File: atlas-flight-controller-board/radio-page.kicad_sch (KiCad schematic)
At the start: 1 part

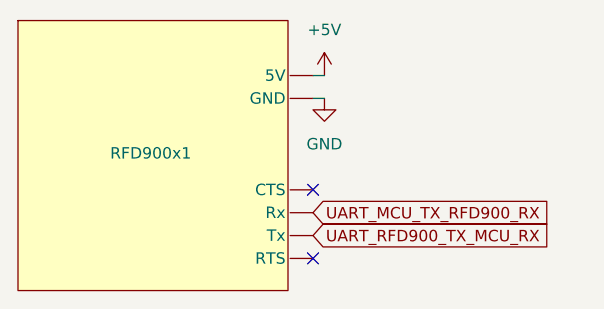
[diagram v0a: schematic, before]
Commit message: Added Regulator, Leaving disconnected, and off pcb for now as teensy board does this automatically. Leaving on for future revs without teensy board
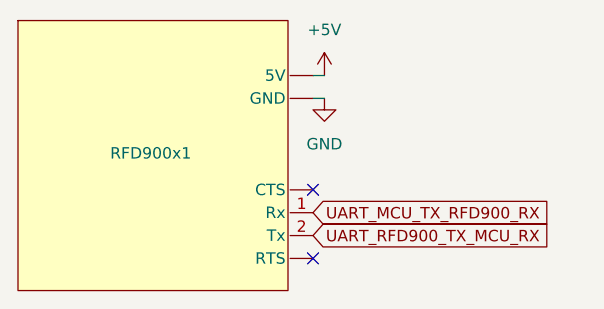
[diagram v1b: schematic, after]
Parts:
- RFD900x1: footprint (none) -> TerminalBlock:TerminalBlock_Xinya_XY308-2.54-2P_1x02_P2.54mm_Horizontal
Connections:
- net UART_MCU_TX_RFD900_RX: now also RFD900x1.1 (Rx); no longer RFD900x1. (RTS)
- net UART_RFD900_TX_MCU_RX: now also RFD900x1.2 (Tx); no longer RFD900x1. (RTS)
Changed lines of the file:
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@@
 			)
 		)
-		(property "Footprint" ""
+		(property "Footprint" "TerminalBlock:TerminalBlock_Xinya_XY308-2.54-2P_1x02_P2.54mm_Horizontal"
 			(at 134.62 93.98 0)
 			(effects
@@
 			)
 		)
-		(pin ""
+		(pin "1"
 		)
 		(pin ""
@@
 		(pin ""
 		)
-		(pin ""
+		(pin "2"
 		)
 		(pin ""

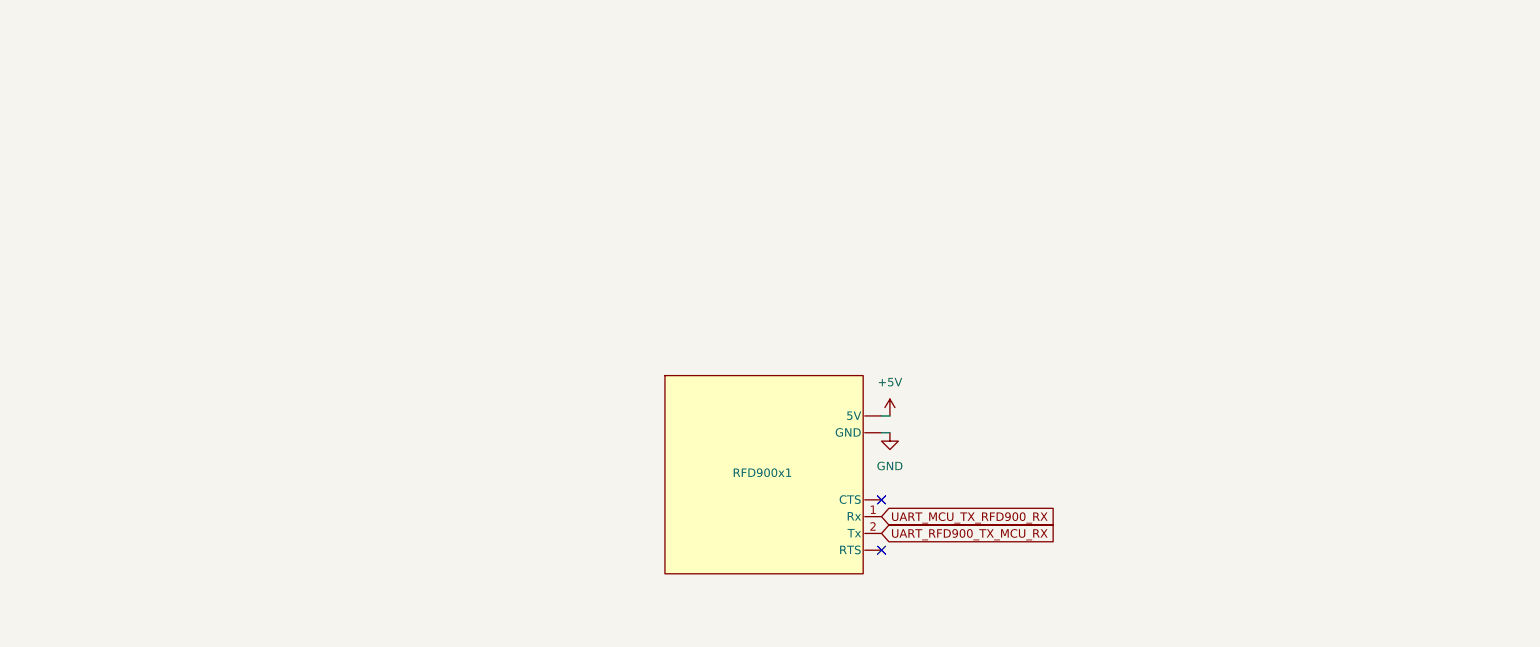
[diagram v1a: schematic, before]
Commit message: Updating IMU to SPI
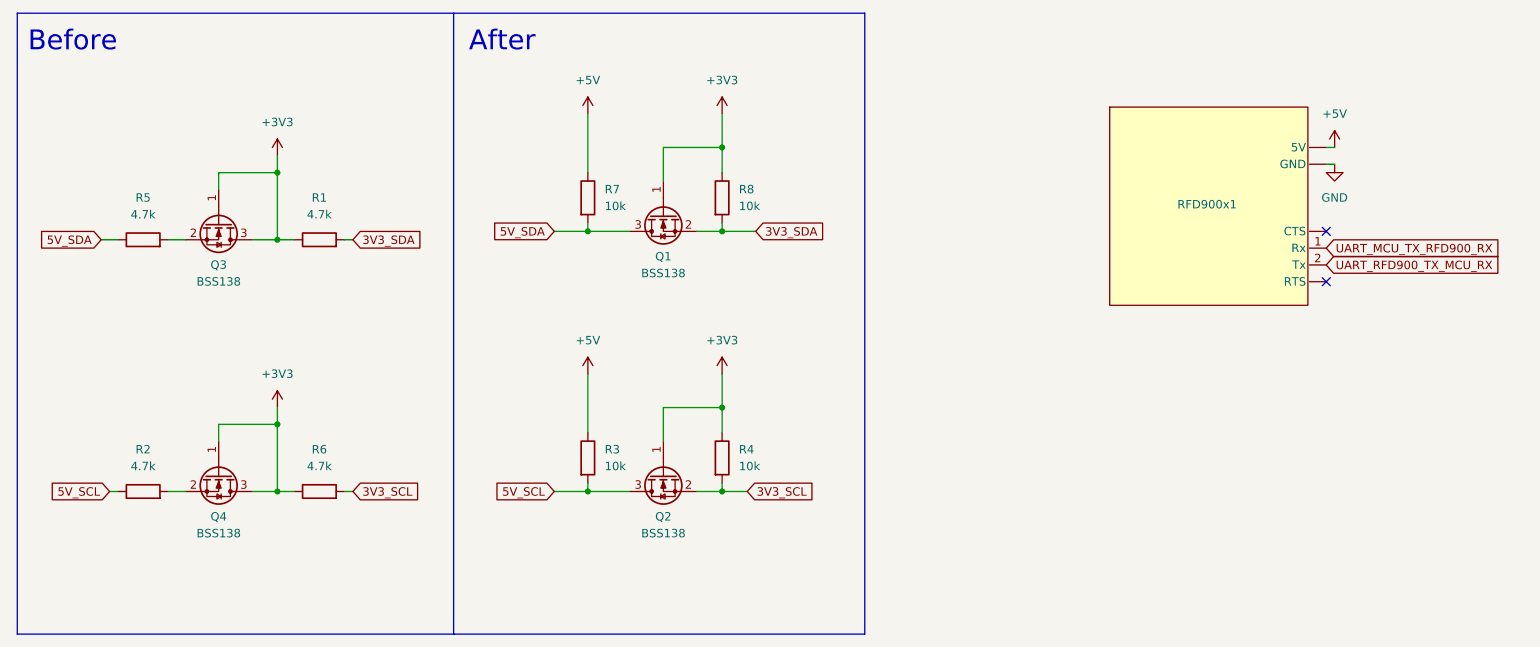
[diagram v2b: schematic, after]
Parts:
- added Q1, Q2, Q3, Q4: BSS138, Package_TO_SOT_SMD:SOT-23, symbol Transistor_FET:BSS138
- added R1, R2, R5, R6: 4.7k, symbol Device:R
- added R3, R4, R7, R8: 10k, symbol Device:R
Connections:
- net +5V: now also R3.1, R7.1
- new net: Q4.2 (S), R2.2
- new net: Q3.2 (S), R5.2
- new net +3V3: Q1.1 (G), Q2.1 (G), Q3.1 (G), Q3.3 (D), Q4.1 (G), Q4.3 (D), R1.1, R4.1, R6.1, R8.1
- new net 3V3_SCL: Q2.2 (S), R4.2, R6.2
- new net 3V3_SDA: Q1.2 (S), R1.2, R8.2
- new net 5V_SCL: Q2.3 (D), R2.1, R3.2
- new net 5V_SDA: Q1.3 (D), R5.1, R7.2
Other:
- note added: "After"
- note added: "Before"
- moved on the sheet: RFD900x1

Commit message: removing some olds symbols, adding some new things such as nand flash chip.
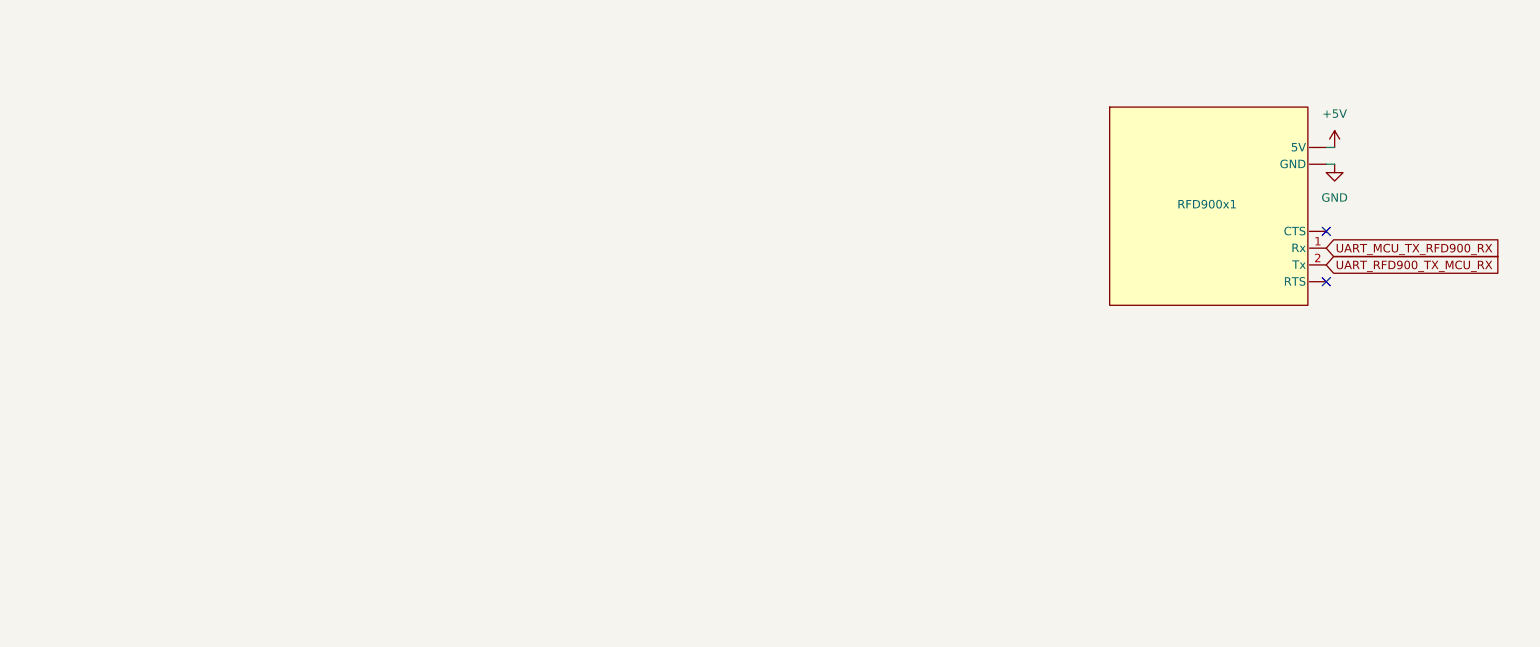
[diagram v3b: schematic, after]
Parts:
- removed Q1, Q2, Q3, Q4: BSS138, Package_TO_SOT_SMD:SOT-23, symbol Transistor_FET:BSS138
- removed R1, R2, R5, R6: 4.7k, symbol Device:R
- removed R3, R4, R7, R8: 10k, symbol Device:R
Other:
- note removed: "After"
- note removed: "Before"
